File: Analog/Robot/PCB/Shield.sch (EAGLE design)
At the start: 5 parts, among them IC2 LM2574HVN-3.3

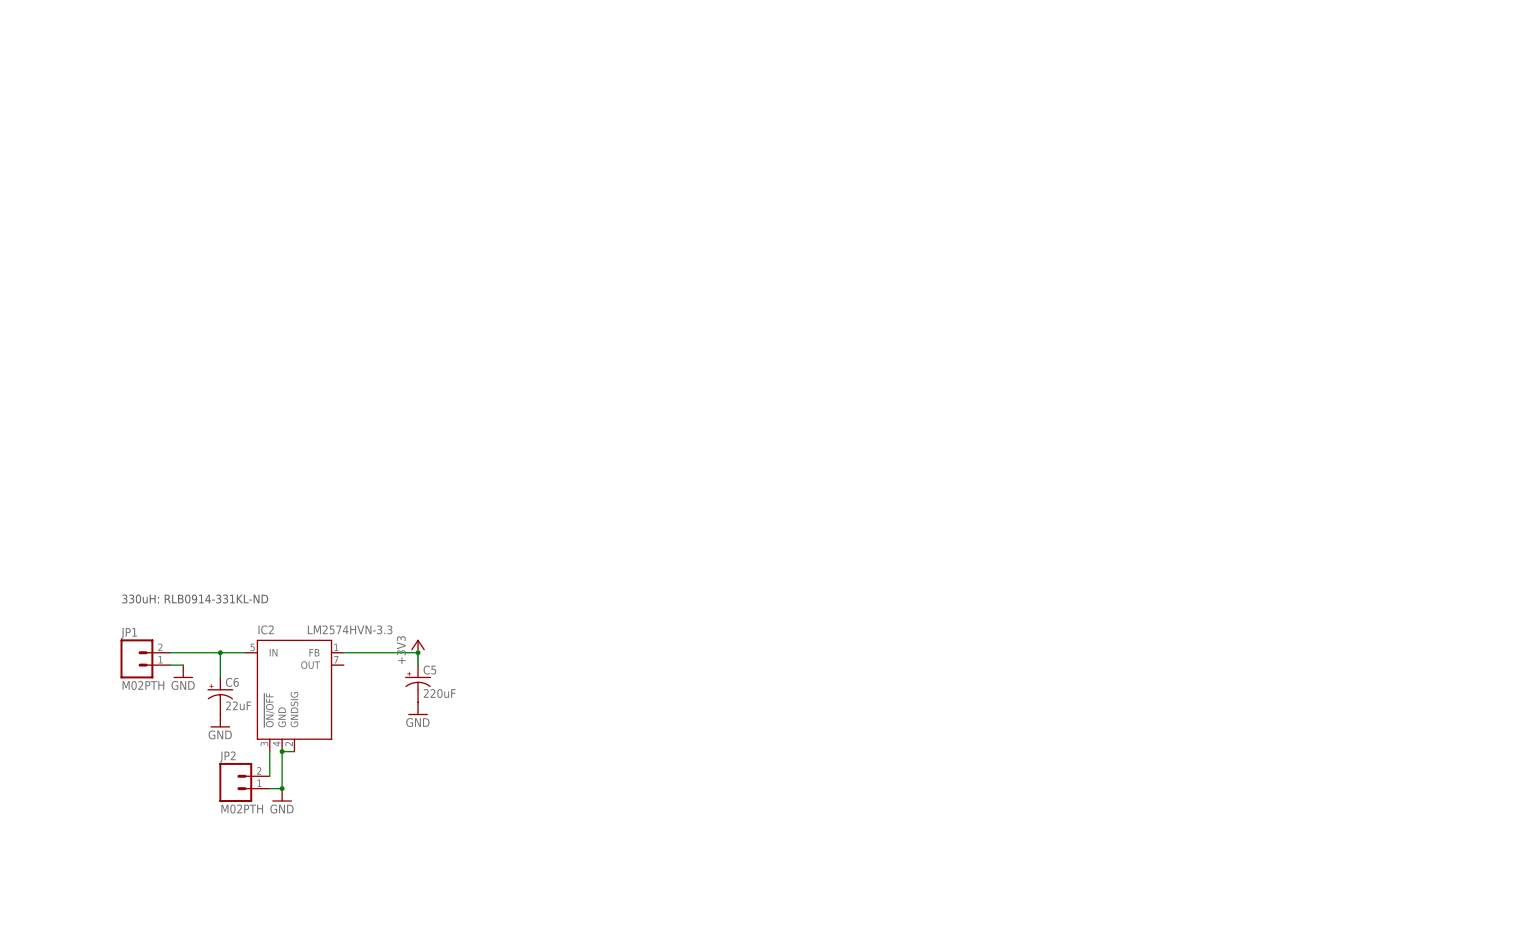
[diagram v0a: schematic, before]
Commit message: PCB and firmware
Gate PCB 70% completed, need to figure out pinout for MCU and layout
signal amps.  Board size reduced by 50%.  Also need to add testpoints
Robot PCB PSU layout completed, motor and stepper drivers will move to
separate PCB
Created firmware files, w/o code
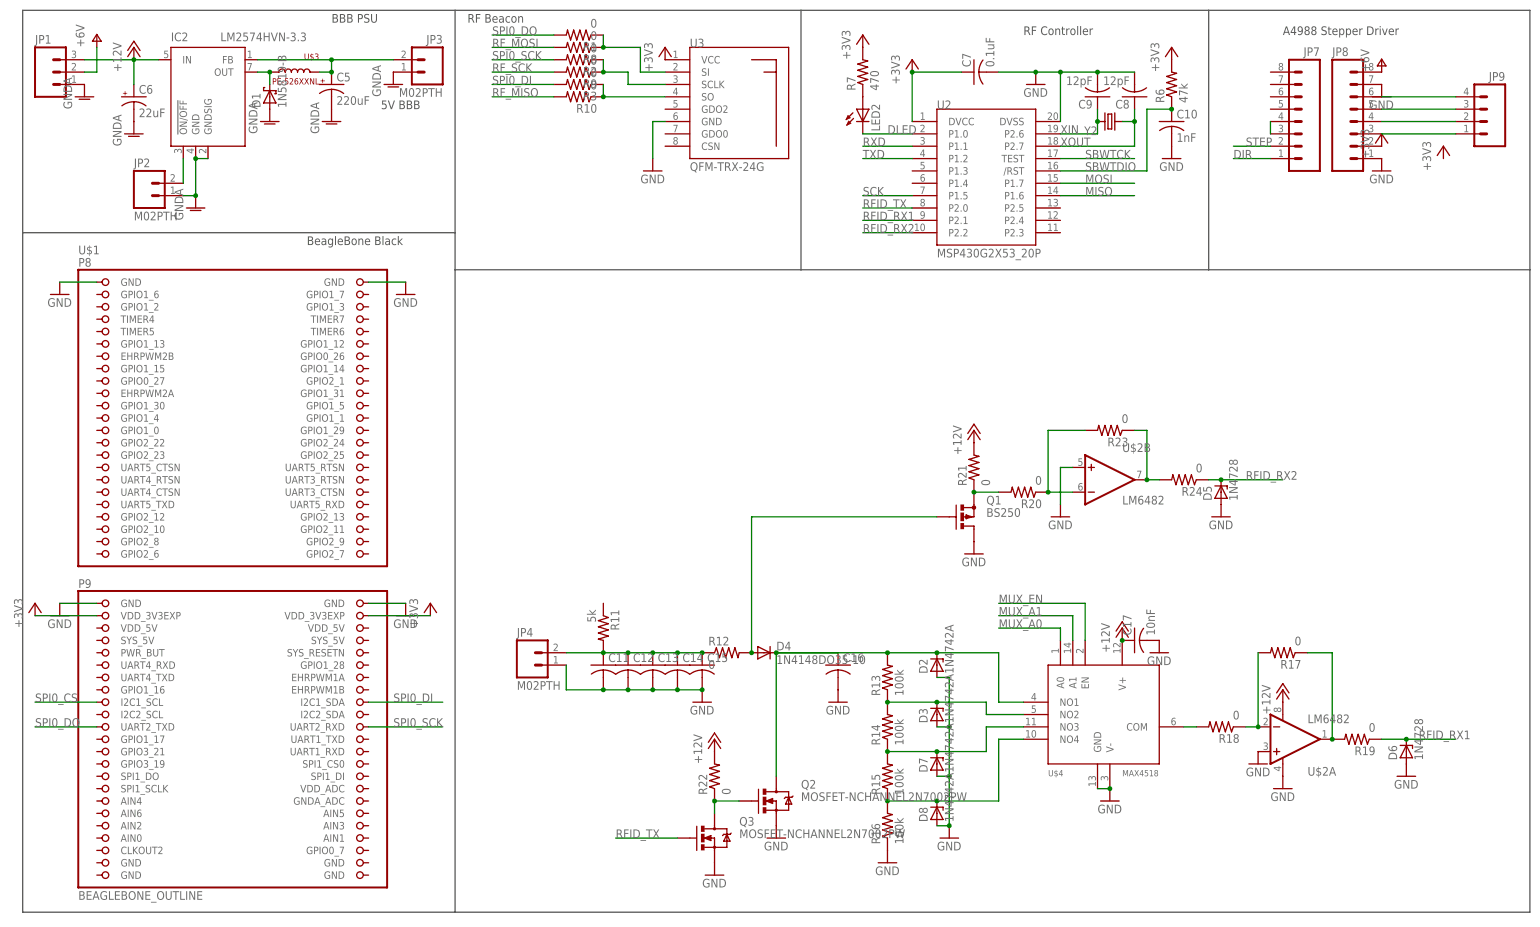
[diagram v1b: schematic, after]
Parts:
- added C10: 1nF, rcl:C-USC0805
- added C11, C12, C13, C14, C15, C16: (no value), rcl:C-USC0805
- added C17: 10nF, rcl:C-USC0805
- added C7: 0.1uF, rcl:C-USC0805
- added C8, C9: 12pF, rcl:C-USC0805
- added D1: 1N5819-B, diode:1N5819-B
- added D2, D3, D7, D8: 1N4742A, diode:1N4728
- added D4: 1N4148DO35-10, diode:1N4148DO35-10
- added D5, D6: 1N4728, diode:1N4728
- added JP3, JP4: M02PTH, SparkFun-Connectors:M02PTH
- added JP7, JP8: (no value), SparkFun-Connectors:M081X08
- added JP9: (no value), SparkFun-Connectors:M04PTH
- added LED2: (no value), led:LEDCHIP-LED0805
- added Q1: BS250, transistor-small-signal:BS250
- added Q2, Q3: MOSFET-NCHANNEL2N7002PW, SparkFun-DiscreteSemi:MOSFET-NCHANNEL2N7002PW
- added R1, R10, R12, R17, R18, R19, R2, R20, R21, R22, R23, R24, R3, R8, R9: 0, rcl:R-US_R0805
- added R11: 5k, rcl:R-US_R0805
- added R13, R14, R15, R16: 100k, rcl:R-US_R0805
- added R6: 47k, rcl:R-US_R0805
- added R7: 470, rcl:R-US_R0805
- added U$1: BEAGLEBONE_OUTLINE, adafruit:BEAGLEBONE_OUTLINE
- added U$2: LM6482, npol:LM6482
- added U$3: PE-526XXNL, npol:PE-526XXNL
- added U$4: MAX4518, npol:MAX4518
- added U2: MSP430G2X53_20P, npol:MSP430G2X53_20P
- added U3: QFM-TRX-24G, npol:QFM-TRX-24G
- added Y2: (no value), SparkFun-FreqCtrl:CRYSTALHC49UV
- JP1: value M02PTH -> (none); device SparkFun-Connectors:M02PTH -> SparkFun-Connectors:M03PTH
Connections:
- new net +12V: C17.1, C6.+, IC2.IN, JP1.3, R21.2, R22.2, U$2A.V+, U$4.V+
- new net DIR: JP7.1
- new net DLED: LED2.C, U2.P1.0
- new net GNDA: C5.-, C6.-, D1.A, IC2.GND@PWR, IC2.GNDSIG, JP1.1, JP2.1, JP3.1
- new net MISO: U2.P1.6
- new net MOSI: U2.P1.7
- new net MUX_A0: U$4.A0
- new net MUX_A1: U$4.A1
- new net MUX_EN: U$4.EN
- new net N$10: D4.A, Q1.G, R12.2
- new net N$11: C16.1, D2.C, D4.C, Q2.D, R13.2, U$4.NO1
- new net N$12: R20.1, R23.2, U$2B.-IN
- new net N$13: R23.1, R24.2, U$2B.OUT
- new net N$14: R18.2, U$4.COM
- new net N$15: R17.2, R18.1, U$2A.-IN
- new net N$16: R17.1, R19.2, U$2A.OUT
- new net N$17: JP7.3, JP7.4
- new net N$18: D3.C, R13.1, R14.2, U$4.NO2
- new net N$19: D7.C, R14.1, R15.2, U$4.NO3
- new net N$2: LED2.A, R7.1
- new net N$20: D8.C, R15.1, R16.2, U$4.NO4
- new net N$21: Q1.S, R20.2, R21.1
- new net N$22: Q2.G, Q3.D, R22.1
- new net N$26: JP8.3, JP9.1
- new net N$27: JP8.4, JP9.2
- new net N$28: JP8.5, JP9.3
- new net N$29: JP8.6, JP9.4
- new net N$3: D1.C, IC2.OUT, U$3.P$2
- new net N$4: C5.+, IC2.FB, JP3.2, U$3.P$1
- new net N$7: R2.1, R9.1, U3.SCLK
- new net N$8: R1.1, R8.1, U3.SI
- new net N$9: C11.1, C12.1, C13.1, C14.1, C15.1, JP4.2, R11.2, R12.1
- new net RFID_RX1: D6.C, R19.1, U2.P2.1
- new net RFID_RX2: D5.C, R24.1, U2.P2.2
- new net RFID_TX: Q3.G, U2.P2.0
- new net RF_MISO: R10.2
- new net RF_MOSI: R8.2
- new net RF_SCK: R9.2
- new net RXD: U2.P1.1
- new net SBWTCK: U2.TEST
- new net SBWTDIO: C10.1, R6.1, U2./RST
- new net SCK: U2.P1.5
- new net SPI0_CS: U$1.I2C1_SCL
- new net SPI0_DI: R3.2, U$1.I2C1_SDA
- new net SPI0_DO: R1.2, U$1.UART2_TXD
- new net SPI0_SCK: R2.2, U$1.UART2_RXD
- new net STEP: JP7.2
- new net TXD: U2.P1.2
- new net V+: JP1.2, JP8.8
- new net XIN: C9.1, U2.P2.6, Y2.2
- new net XOUT: C8.1, U2.P2.7, Y2.1
- net +3V3: now also C7.1, JP8.2, R6.2, R7.2, U$1.VDD_3V3EXP@1, U$1.VDD_3V3EXP@2, U2.DVCC, U3.VCC; no longer C5.+, IC2.FB
- net GND: now also C10.2, C11.2, C12.2, C13.2, C14.2, C15.2, C16.2, C17.2, C7.2, C8.2, C9.2, D2.A, D3.A, D5.A, D6.A, D7.A, D8.A, JP4.1, JP8.1, JP8.7, Q1.D, Q2.S, Q3.S, R16.1, U$1.GND@1, U$1.GND@2, U$1.GND@7, U$1.GND@8, U$2A.+IN, U$2A.V-, U$2B.+IN, U$4.GND, U$4.V-, U2.DVSS, U3.GND; no longer C5.-, C6.-, IC2.GND@PWR, IC2.GNDSIG, JP1.1, JP2.1
- net N$5: now also R10.1, R3.1, U3.SO; no longer C6.+, IC2.IN, JP1.2
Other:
- note added: "5V BBB"
- note added: "A4988 Stepper Driver"
- note added: "BBB PSU"
- note added: "BeagleBone Black"
- note added: "RF Beacon"
- note added: "RF Controller"
- note removed: "330uH: RLB0914-331KL-ND"
- moved on the sheet: C5, C6, IC2, JP2

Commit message: Board final; SPI progress
Sent PCBs to FAB
SPI driver working for multi-byte.  Bug: bytes are sent in reversed
order, although bit ordering (MSB first) is correct.
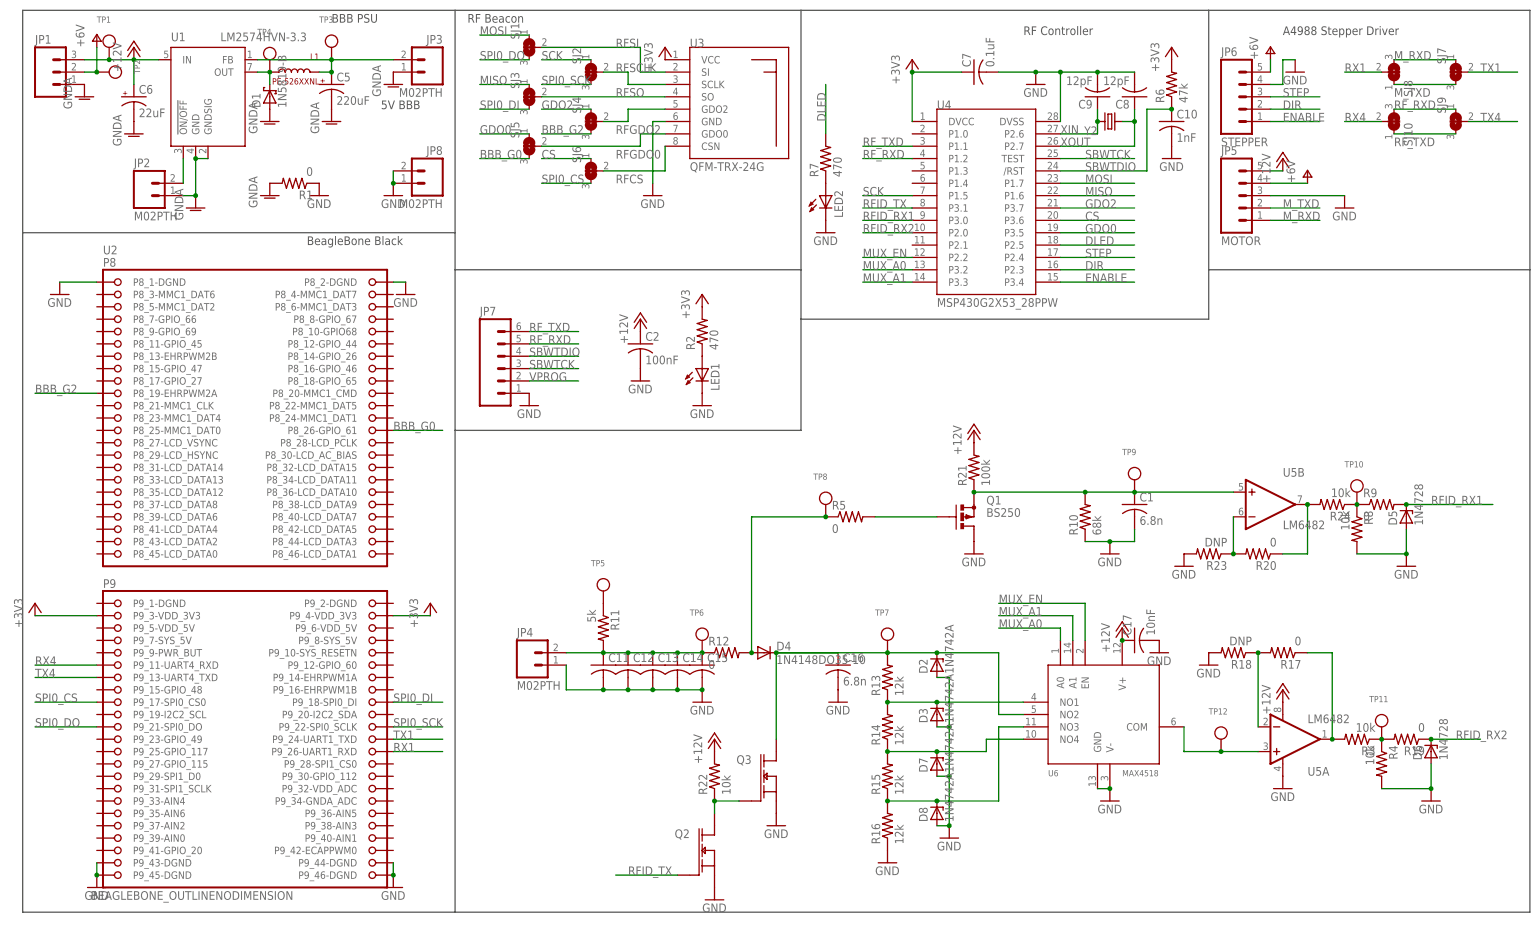
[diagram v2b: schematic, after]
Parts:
- removed JP9: (no value), SparkFun-Connectors:M04PTH
- removed U$1: BEAGLEBONE_OUTLINE, adafruit:BEAGLEBONE_OUTLINE
- removed U$4: MAX4518, npol:MAX4518
- added C1: 6.8n, rcl:C-USC0805
- added C2: 100nF, rcl:C-USC0805
- added JP5: MOTOR, SparkFun-Connectors:M05PTH
- added JP6: STEPPER, SparkFun-Connectors:M05PTH
- added LED1: (no value), led:LEDCHIP-LED0805
- added R4: 10k, rcl:R-US_R0805
- added R5: 0, rcl:R-US_R0805
- added SJ1, SJ10, SJ2, SJ3, SJ4, SJ5, SJ6, SJ7, SJ8, SJ9: (no value), microbuilder:SOLDERJUMPER_2WAY0805
- added TP1, TP10, TP11, TP12, TP2, TP3, TP4, TP5, TP6, TP7, TP8, TP9: (no value), microbuilder:TESTPOINT0.1"
- added U4: MSP430G2X53_28PPW, npol:MSP430G2X53_28PPW
- added U6: MAX4518, npol:MAX4518
- C16: value (none) -> 6.8n
- JP7: device SparkFun-Connectors:M081X08 -> SparkFun-Connectors:M06SIP
- JP8: value (none) -> M02PTH; device SparkFun-Connectors:M081X08 -> SparkFun-Connectors:M02PTH
- Q2, Q3: value MOSFET-NCHANNEL2N7002PW -> 2N7002_SINGLESOT23/TO-236AB; device SparkFun-DiscreteSemi:MOSFET-NCHANNEL2N7002PW -> npol:2N7002_SINGLESOT23/TO-236AB
- R10: value 0 -> 68k
- R13, R14, R15, R16: value 100k -> 12k
- R18, R23: value 0 -> DNP
- R2: value 0 -> 470
- R21: value 0 -> 100k
- R22, R24, R3, R8: value 0 -> 10k
- U2: value MSP430G2X53_20P -> BEAGLEBONE_OUTLINENODIMENSION; device npol:MSP430G2X53_20P -> npol:BEAGLEBONE_OUTLINENODIMENSION
- renumbered IC2 to U1, U$2 to U5, U$3 to L1
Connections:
- removed net N$14 (its old number): R18.2, U$4.COM
- removed net N$26: JP8.3, JP9.1
- removed net N$28: JP8.5, JP9.3
- removed net N$29: JP8.6, JP9.4
- removed net N$5: R10.1, R3.1, U3.SO
- removed net N$7: R2.1, R9.1, U3.SCLK
- removed net RF_MISO: R10.2
- removed net RF_MOSI: R8.2
- removed net RF_SCK: R9.2
- removed net RXD: U2.P1.1
- removed net TXD: U2.P1.2
- new net BBB_G0: SJ5.3, U2.P8_26-GPIO_61
- new net BBB_G2: SJ4.3, U2.P8_19-EHRPWM2A
- new net CS: SJ6.1, U4.P3.6
- new net ENABLE: JP6.1, U4.P3.4
- new net GDO0: SJ5.1, U4.P3.5
- new net GDO2: SJ4.1, U4.P3.7
- new net M_RXD: JP5.1, SJ7.1, SJ8.3
- new net M_TXD: JP5.2, SJ7.3, SJ8.1
- new net N$1: R11.1, TP5.P$1
- new net N$15: R24.1, R8.1, R9.1, TP10.P$1
- new net N$23: Q1.G, R5.2
- new net RFCS: SJ6.2, U3.CSN
- new net RFGDO0: SJ5.2, U3.GDO0
- new net RFGDO2: SJ4.2, U3.GDO2
- new net RFSCLK: SJ2.2, U3.SCLK
- new net RFSI: SJ1.2, U3.SI
- new net RFSO: SJ3.2, U3.SO
- new net RF_RXD: JP7.5, SJ10.3, SJ9.1, U4.P1.2
- new net RF_TXD: JP7.6, SJ10.1, SJ9.3, U4.P1.1
- new net RX1: SJ8.2, U2.P9_26-UART1_RXD
- new net RX4: SJ10.2, U2.P9_11-UART4_RXD
- new net TX1: SJ7.2, U2.P9_24-UART1_TXD
- new net TX4: SJ9.2, U2.P9_13-UART4_TXD
- new net VPROG: JP7.2
- net +12V: now also C2.1, JP5.5, TP1.P$1, U6.V+; no longer U$4.V+
- net +3V3: now also R2.2, U2.P9_3-VDD_3V3, U2.P9_4-VDD_3V3, U4.DVCC; no longer JP8.2, R7.2, U$1.VDD_3V3EXP@1, U$1.VDD_3V3EXP@2, U2.DVCC
- net DIR: now also JP6.2, U4.P2.3; no longer JP7.1
- net DLED: now also R7.2, U4.P2.5; no longer LED2.C, U2.P1.0
- net GND: now also C1.2, C2.2, JP5.3, JP6.4, JP7.1, JP8.2, LED1.C, LED2.C, R1.1, R10.1, R18.2, R23.2, R4.2, R8.2, U2.P8_1-DGND, U2.P8_2-DGND, U2.P9_43-DGND, U2.P9_44-DGND, U2.P9_45-DGND, U2.P9_46-DGND, U4.DVSS, U6.GND, U6.V-; no longer JP8.7, U$1.GND@1, U$1.GND@2, U$1.GND@7, U$1.GND@8, U$4.GND, U$4.V-, U2.DVSS, U5A.+IN, U5B.+IN
- net GNDA: now also R1.2
- net MISO: now also SJ3.1, U4.P1.6; no longer U2.P1.6
- net MOSI: now also SJ1.1, U4.P1.7; no longer U2.P1.7
- net MUX_A0: now also U4.P3.2, U6.A0; no longer U$4.A0
- net MUX_A1: now also U4.P3.3, U6.A1; no longer U$4.A1
- net MUX_EN: now also U4.P2.2, U6.EN; no longer U$4.EN
- net N$10: now also R5.1, TP8.P$1; no longer Q1.G
- net N$11: now also Q3.D, TP7.P$1, U6.NO2; no longer Q2.D, U$4.NO1
- net N$12: now also R20.2, R23.1; no longer R20.1, R23.2
- net N$13: now also R20.1; no longer R23.1
- net N$16: now also R3.2; no longer R19.2
- net N$17: now also R19.2, R3.1, R4.1, TP11.P$1; no longer JP7.3, JP7.4
- net N$18: now also U6.NO1; no longer U$4.NO2
- net N$19: now also U6.NO4; no longer U$4.NO3
- net N$20: now also U6.NO3; no longer U$4.NO4
- net N$21: now also C1.1, R10.2, TP9.P$1, U5B.+IN; no longer R20.2
- net N$22: now also Q2.D, Q3.G; no longer Q2.G, Q3.D
- net N$27: now also LED1.A, R2.1; no longer JP8.4, JP9.2
- net N$3: now also TP4.P$1
- net N$4: now also TP3.P$1
- net N$8: now also TP12.P$1, U5A.+IN, U6.COM; no longer R1.1, R8.1, U3.SI
- net N$9: now also TP6.P$1
- net RFID_RX1: now also D5.C, R9.2, U4.P3.0; no longer D6.C, R19.1, U2.P2.1
- net RFID_RX2: now also D6.C, R19.1, U4.P2.0; no longer D5.C, R24.1, U2.P2.2
- net RFID_TX: now also Q2.G, U4.P3.1; no longer Q3.G, U2.P2.0
- net SBWTCK: now also JP7.3, U4.TEST; no longer U2.TEST
- net SBWTDIO: now also JP7.4, U4./RST; no longer U2./RST
- net SCK: now also SJ2.1, U4.P1.5; no longer U2.P1.5
- net SPI0_CS: now also SJ6.3, U2.P9_17-SPI0_CS0; no longer U$1.I2C1_SCL
- net SPI0_DI: now also SJ3.3, U2.P9_18-SPI0_DI; no longer R3.2, U$1.I2C1_SDA
- net SPI0_DO: now also SJ1.3, U2.P9_21-SPI0_DO; no longer R1.2, U$1.UART2_TXD
- net SPI0_SCK: now also SJ2.3, U2.P9_22-SPI0_SCLK; no longer R2.2, U$1.UART2_RXD
- net STEP: now also JP6.3, U4.P2.4; no longer JP7.2
- net V+: now also JP5.4, JP6.5, TP2.P$1; no longer JP8.8
- net XIN: now also U4.P2.6; no longer U2.P2.6
- net XOUT: now also U4.P2.7; no longer U2.P2.7
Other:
- note added: "Motor Driver"
- moved on the sheet: D5, D6, LED2, R1, R10, R18, R19, R2, R20, R23, R24, R3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
